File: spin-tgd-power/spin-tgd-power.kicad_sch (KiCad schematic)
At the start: 13 parts, among them J1 FT_switch, J10 Conn_01x01, J11 Conn_01x01, J2 bat_high, J3 bat_low, J4 Conn_01x01, J5 Conn_01x01, J6 Conn_01x01, J7 Conn_01x01, J8 ESC_Foo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

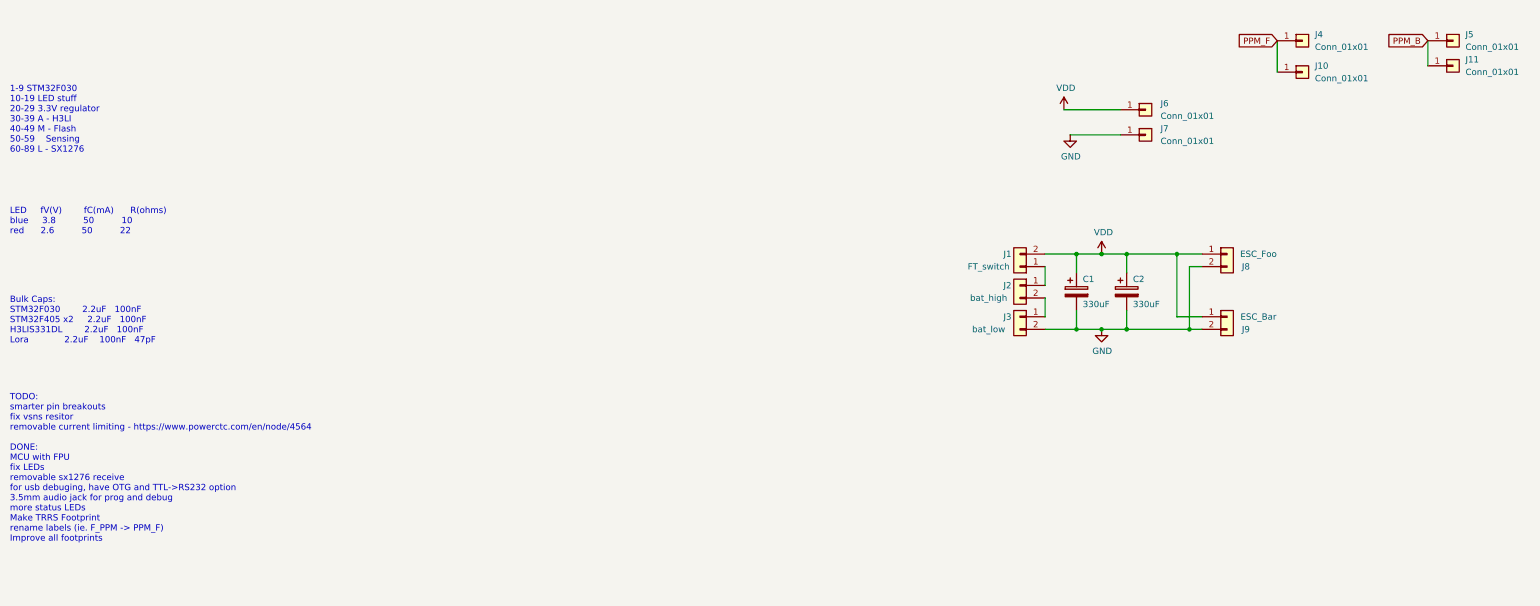
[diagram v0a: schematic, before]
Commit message: DSP DAC circuit and FO card todo notes
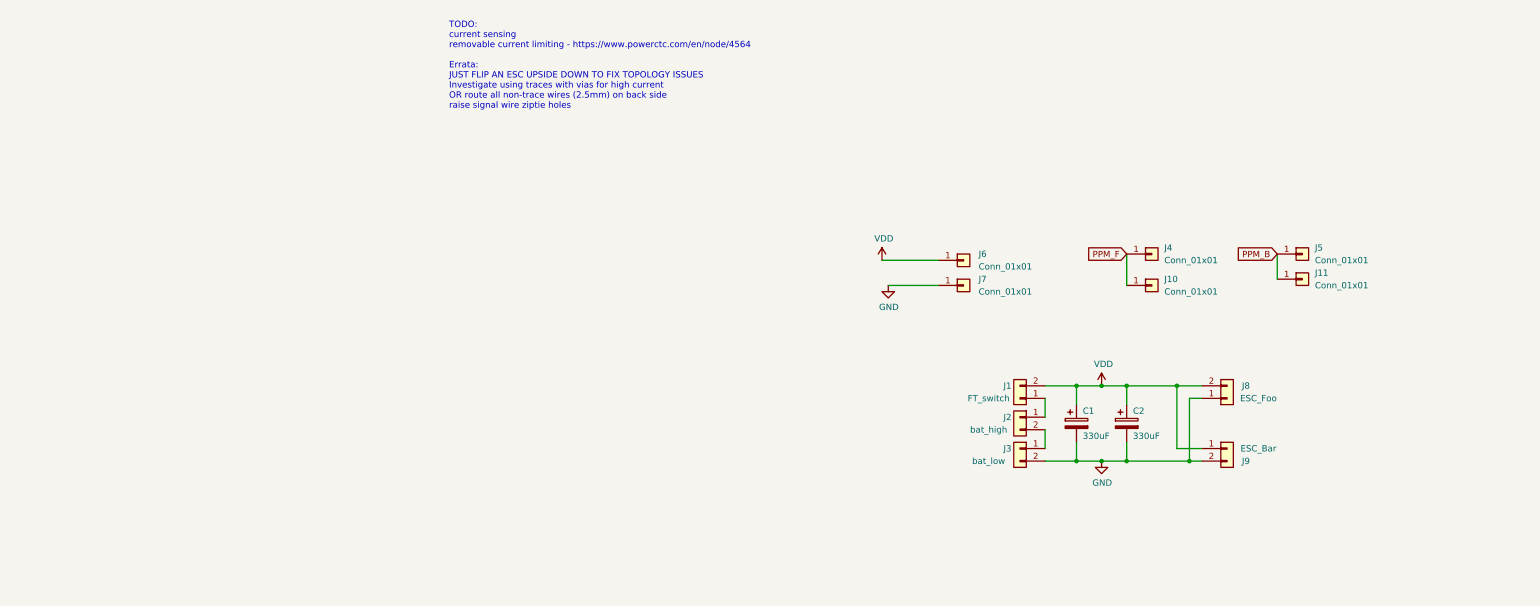
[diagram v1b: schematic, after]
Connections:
- net GND: now also J8.1 (Pin_1); no longer J8.2 (Pin_2)
- net VDD: now also J8.2 (Pin_2); no longer J8.1 (Pin_1)
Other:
- note added: "TODO: current sensing removable current limiting - https://www.powerctc.com/en/node/4564 Errata: JUST FLIP AN ESC UPSIDE DOWN TO FIX TOPOLOGY ISSUES Investigate using traces with vias for high current OR route all non-trace wires (2.5mm) on back side raise signal wire ziptie holes"
- note removed: "1-9 STM32F030 10-19 LED stuff 20-29 3.3V regulator 30-39 A - H3LI 40-49 M - Flash 50-59 Sensing 60-89 L - SX1276"
- note removed: "Bulk Caps: STM32F030 2.2uF 100nF STM32F405 x2 2.2uF 100nF H3LIS331DL 2.2uF 100nF Lora 2.2uF 100nF 47pF"
- note removed: "LED fV(V) fC(mA) R(ohms) blue 3.8 50 10 red 2.6 50 22"
- note removed: "TODO: smarter pin breakouts fix vsns resitor removable current limiting - https://www.powerctc.com/en/node/4564 DONE: MCU with FPU fix LEDs removable sx1276 receive for usb debuging, have OTG and TTL->RS232 option 3.5mm audio jack for prog and debug more status LEDs Make TRRS Footprint rename labels (ie. F_PPM -> PPM_F) Improve all footprints"
- moved on the sheet: C1, C2, J1, J10, J11, J2, J3, J4, J5, J6, J7, J8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

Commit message: Moved to new library system
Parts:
- added C?: 1uF?, symbol Device:C
- added Q?: Q_PMOS_GSD, symbol Device:Q_PMOS_GSD
- added R?: 0.005R?, symbol Device:R
- added R?: 10K?, symbol Device:R
- added R?: 20K?, symbol Device:R
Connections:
- net GND: now also R?.2
- net VDD: now also R?.2; no longer J1.2 (Pin_2)
- new net: Q?.3 (D), R?.1
- new net: C?.1, J1.2 (Pin_2), Q?.2 (S), R?.1
- new net: C?.2, Q?.1 (G), R?.1, R?.2
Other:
- note added: "70A/4096 = 0.017A per div, but you def need an amp for this."
- note added: "TODO: current sensing removable current limiting - https://www.powerctc.com/en/node/4564 Errata: JUST FLIP AN ESC UPSIDE DOWN TO FIX TOPOLOGY ISSUES Investigate using traces with vias for high current 10mm 2oz traces on both layers should carry enough current OR route all non-trace wires (2.5mm) on back side raise signal wire ziptie holes XT-30 FP polarity is wrong"
- note removed: "TODO: current sensing removable current limiting - https://www.powerctc.com/en/node/4564 Errata: JUST FLIP AN ESC UPSIDE DOWN TO FIX TOPOLOGY ISSUES Investigate using traces with vias for high current OR route all non-trace wires (2.5mm) on back side raise signal wire ziptie holes"
- moved on the sheet: C1, C2, J1, J2, J3, J8, J9

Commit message: Eggman V2 ordered gerbers
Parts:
- removed C?: 1uF?, symbol Device:C
- removed J10, J11, J4, J7: Conn_01x01, lib_fp:TGD-antenna-THT, symbol Connector_Generic:Conn_01x01
- removed Q?: Q_PMOS_GSD, symbol Device:Q_PMOS_GSD
- removed R?: 0.005R?, symbol Device:R
- removed R?: 10K?, symbol Device:R
- removed R?: 20K?, symbol Device:R
- added C3: 4.7nF, Capacitor_SMD:C_0603_1608Metric, symbol Device:C
- added D1: ZMM3V3, Diode_SMD:D_MiniMELF, symbol Device:D_Zener
- added J4: Conn_01x05, Connector_JST:JST_EH_B5B-EH-A_1x05_P2.50mm_Vertical, symbol Connector_Generic:Conn_01x05
- added R1: 0.0025R, Resistor_SMD:R_2512_6332Metric_Pad1.40x3.35mm_HandSolder, symbol Device:R
- added R2: 100R, Resistor_SMD:R_0603_1608Metric, symbol Device:R
- added R3: 1K, Resistor_SMD:R_0603_1608Metric, symbol Device:R
- added U1: INA185A1, Package_TO_SOT_SMD:SOT-563, symbol AlfredoSymbols:INA185A
- J2, J3: footprint lib_fp:TGD_AMASS_XT30U-F_1x02_P5.0mm_Vertical -> AlfredoFootprints:TGD_2P_BatHoles
- J5, J6: footprint lib_fp:TGD-antenna-THT -> AlfredoFootprints:TGD-antenna-THT
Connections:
- net GND: now also C3.1, D1.2 (A), J4.2 (Pin_2), R1.2, U1.2 (GND), U1.4 (IN-), U1.5 (REF); no longer C1.2, C2.2, J8.1 (Pin_1), J9.2 (Pin_2)
- net PPM_B: now also J4.4 (Pin_4)
- net PPM_F: now also J6.1 (Pin_1), J4.5 (Pin_5)
- net VDD: now also J1.2 (Pin_2), J4.3 (Pin_3), R3.1; no longer J6.1 (Pin_1)
- new net: R2.2, U1.1 (Out)
- new net +3V3: D1.1 (K), R3.2, U1.6 (VS)
- new net CurSns: C3.2, J4.1 (Pin_1), R2.1
- new net sns+: C1.2, C2.2, J8.1 (Pin_1), J9.2 (Pin_2), R1.1, U1.3 (IN+)
